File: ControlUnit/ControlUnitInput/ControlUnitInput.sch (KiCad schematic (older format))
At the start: 41 parts, among them J1 Conn_02x15_Odd_Even, J2 Conn_01x02, SW1 SW_Push, SW10 SW_Push, SW11 SW_Push, SW12 SW_Push, SW13 SW_Push, SW14 SW_Push, SW15 SW_Push, SW16 SW_Push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

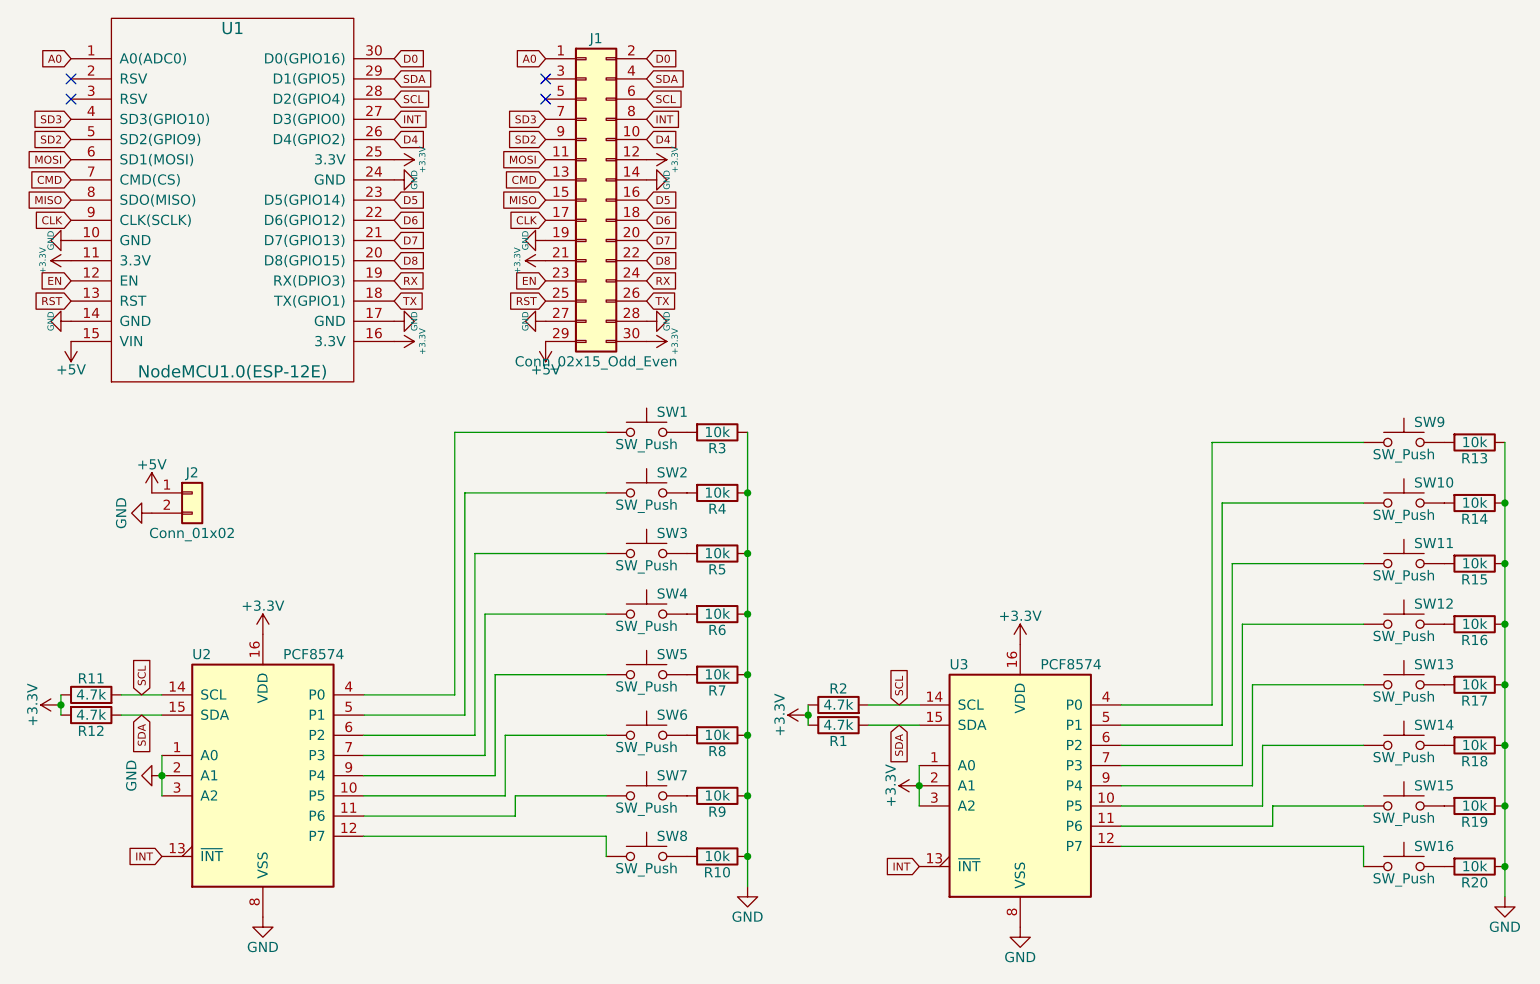
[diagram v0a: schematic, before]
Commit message: add additional connectors for NodeMCU pins in order to be able to connect additional input devices later on
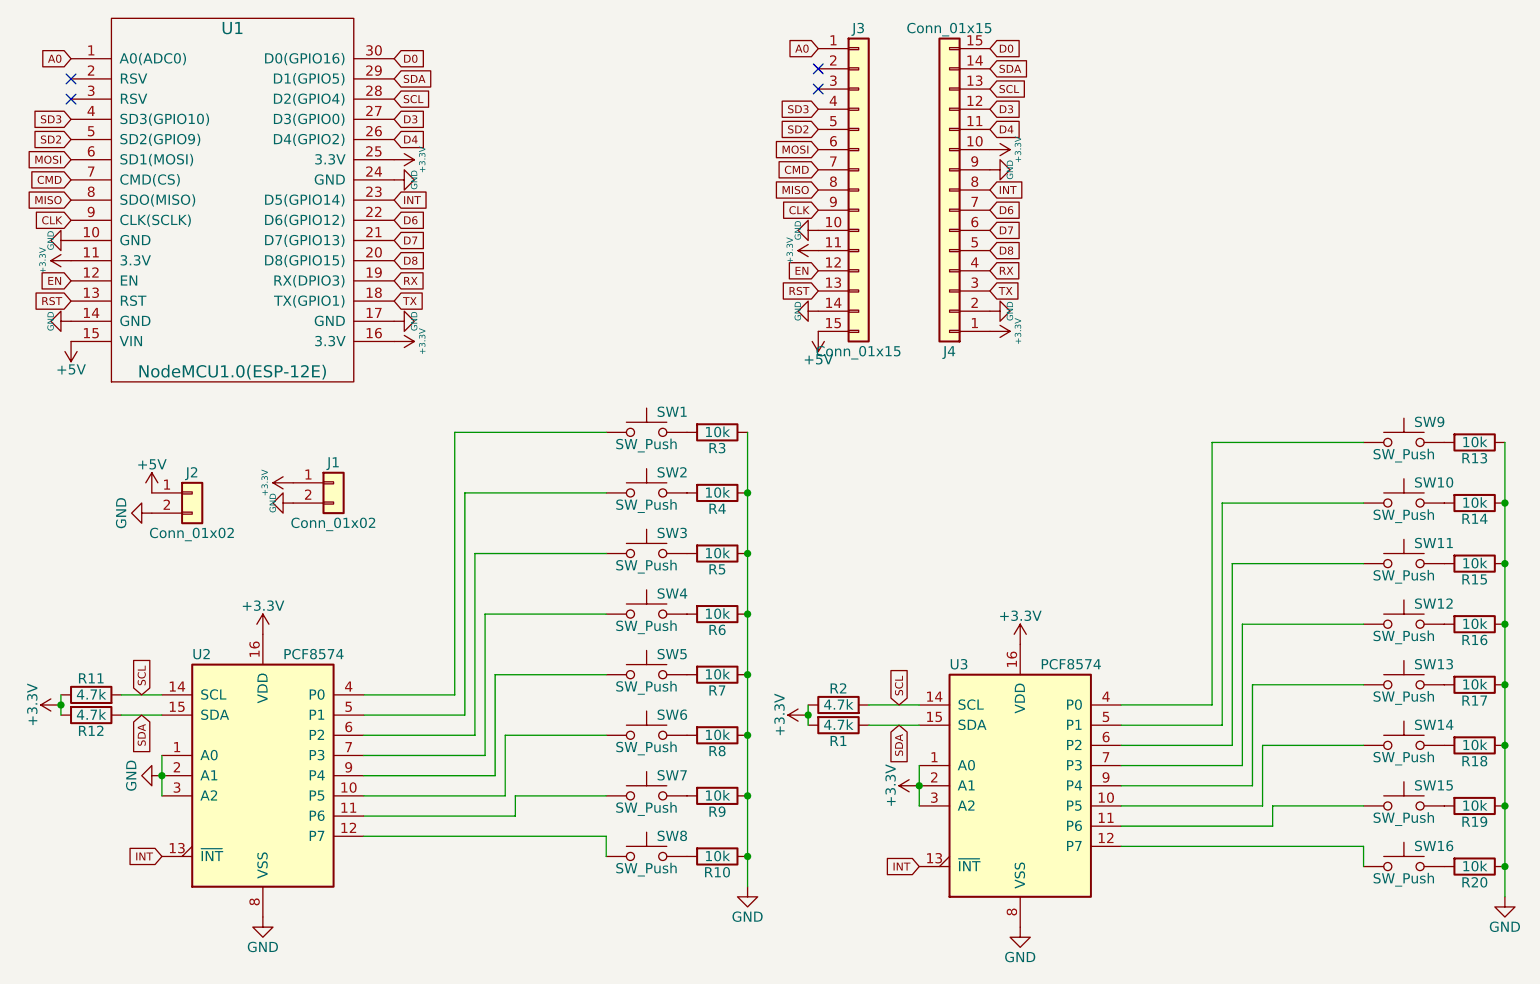
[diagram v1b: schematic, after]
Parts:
- removed J1: Conn_02x15_Odd_Even, Pin_Headers:Pin_Header_Straight_2x15_Pitch2.54mm, symbol Conn_02x15_Odd_Even
- added J1: Conn_01x02, Pin_Headers:Pin_Header_Straight_1x02_Pitch2.54mm, symbol Conn_01x02
- added J3, J4: Conn_01x15, Pin_Headers:Pin_Header_Straight_1x15_Pitch2.54mm, symbol Conn_01x15
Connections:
- net D5 is gone; now on net INT: U1.23 (D5(GPIO14))
- net +3V3: now also J1.1 (Pin_1), J3.11 (Pin_11), J4.1 (Pin_1), J4.10 (Pin_10)
- net +5V: now also J3.15 (Pin_15)
- net A0: now also J3.1 (Pin_1)
- net CLK: now also J3.9 (Pin_9)
- net CMD: now also J3.7 (Pin_7)
- net D0: now also J4.15 (Pin_15)
- net D4: now also J4.11 (Pin_11)
- net D6: now also J4.7 (Pin_7)
- net D7: now also J4.6 (Pin_6)
- net D8: now also J4.5 (Pin_5)
- net EN: now also J3.12 (Pin_12)
- net GND: now also J1.2 (Pin_2), J3.10 (Pin_10), J3.14 (Pin_14), J4.2 (Pin_2), J4.9 (Pin_9)
- net INT: now also J4.8 (Pin_8); no longer U1.27 (D3(GPIO0))
- net MISO: now also J3.8 (Pin_8)
- net MOSI: now also J3.6 (Pin_6)
- net RST: now also J3.13 (Pin_13)
- net RX: now also J4.4 (Pin_4)
- net SCL: now also J4.13 (Pin_13)
- net SD2: now also J3.5 (Pin_5)
- net SD3: now also J3.4 (Pin_4)
- net SDA: now also J4.14 (Pin_14)
- net TX: now also J4.3 (Pin_3)
- new net D3: J4.12 (Pin_12), U1.27 (D3(GPIO0))
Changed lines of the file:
@@
 LIBS:valves
 LIBS:IRLZ34
-LIBS:ws2812b
-LIBS:ESP8266
 LIBS:ControlUnitInput-cache
 EELAYER 25 0
@@
 Text GLabel 2500 950  2    39   Input ~ 0
 SCL
-Text GLabel 2500 1050 2    39   Input ~ 0
+Text GLabel 2500 1450 2    39   Input ~ 0
 INT
 Text GLabel 2500 750  2    39   Input ~ 0
@@
 Text GLabel 2500 1150 2    39   Input ~ 0
 D4
-Text GLabel 2500 1450 2    39   Input ~ 0
-D5
+Text GLabel 2500 1050 2    39   Input ~ 0
+D3
 Text GLabel 2500 1550 2    39   Input ~ 0
 D6
@@
 	0    1    1    0
 $EndComp
-$Comp
-L Conn_02x15_Odd_Even J1
-U 1 1 5A34A10D
-P 3450 1450
-F 0 "J1" H 3500 2250 50  0000 C CNN
-F 1 "Conn_02x15_Odd_Even" H 3500 650 50  0000 C CNN
-F 2 "Pin_Headers:Pin_Header_Straight_2x15_Pitch2.54mm" H 3450 1450 50  0001 C CNN
-F 3 "" H 3450 1450 50  0001 C CNN
-	1    3450 1450
-	1    0    0    -1
-$EndComp
-Text GLabel 3750 750  2    39   Input ~ 0
+Text GLabel 5450 700  2    39   Input ~ 0
 D0
-Text GLabel 3750 850  2    39   Input ~ 0
+Text GLabel 5450 800  2    39   Input ~ 0
 SDA
-Text GLabel 3750 950  2    39   Input ~ 0
+Text GLabel 5450 900  2    39   Input ~ 0
 SCL
-Text GLabel 3750 1050 2    39   Input ~ 0
+Text GLabel 5450 1400 2    39   Input ~ 0
 INT
-Text GLabel 3750 1150 2    39   Input ~ 0
+Text GLabel 5450 1100 2    39   Input ~ 0
 D4
 $Comp
 L GND #PWR06
 U 1 1 5A34A4EF
-P 3750 1350
-F 0 "#PWR06" H 3750 1100 31  0001 C CNN
-F 1 "GND" H 3750 1250 31  0000 C CNN
-F 2 "" H 3750 1350 50  0001 C CNN
-F 3 "" H 3750 1350 50  0001 C CNN
-	1    3750 1350
-	0    -1   -1   0
-$EndComp
-Text GLabel 3750 1450 2    39   Input ~ 0
-D5
-Text GLabel 3750 1550 2    39   Input ~ 0
+P 5450 1300
+F 0 "#PWR06" H 5450 1050 31  0001 C CNN
+F 1 "GND" H 5450 1200 31  0000 C CNN
+F 2 "" H 5450 1300 50  0001 C CNN
+F 3 "" H 5450 1300 50  0001 C CNN
+	1    5450 1300
+	0    -1   -1   0
+$EndComp
+Text GLabel 5450 1000 2    39   Input ~ 0
+D3
+Text GLabel 5450 1500 2    39   Input ~ 0
 D6
-Text GLabel 3750 1650 2    39   Input ~ 0
+Text GLabel 5450 1600 2    39   Input ~ 0
 D7
-Text GLabel 3750 1750 2    39   Input ~ 0
+Text GLabel 5450 1700 2    39   Input ~ 0
 D8
-Text GLabel 3750 1850 2    39   Input ~ 0
+Text GLabel 5450 1800 2    39   Input ~ 0
 RX
-Text GLabel 3750 1950 2    39   Input ~ 0
+Text GLabel 5450 1900 2    39   Input ~ 0
 TX
 $Comp
 L GND #PWR07
 U 1 1 5A34A84E
-P 3750 2050
-F 0 "#PWR07" H 3750 1800 31  0001 C CNN
-F 1 "GND" H 3750 1950 31  0000 C CNN
-F 2 "" H 3750 2050 50  0001 C CNN
-F 3 "" H 3750 2050 50  0001 C CNN
-	1    3750 2050
+P 5450 2000
+F 0 "#PWR07" H 5450 1750 31  0001 C CNN
+F 1 "GND" H 5450 1900 31  0000 C CNN
+F 2 "" H 5450 2000 50  0001 C CNN
+F 3 "" H 5450 2000 50  0001 C CNN
+	1    5450 2000
 	0    -1   -1   0
 $EndComp
@@
 L +5V #PWR08
 U 1 1 5A34A8F9
-P 3250 2150
-F 0 "#PWR08" H 3250 2000 50  0001 C CNN
-F 1 "+5V" H 3250 2290 50  0000 C CNN
-F 2 "" H 3250 2150 50  0001 C CNN
-F 3 "" H 3250 2150 50  0001 C CNN
-	1    3250 2150
+P 4600 2100
+F 0 "#PWR08" H 4600 1950 50  0001 C CNN
+F 1 "+5V" H 4600 2240 50  0000 C CNN
+F 2 "" H 4600 2100 50  0001 C CNN
+F 3 "" H 4600 2100 50  0001 C CNN
+	1    4600 2100
 	-1   0    0    1
 $EndComp
@@
 L GND #PWR09
 U 1 1 5A34A97C
-P 3250 2050
-F 0 "#PWR09" H 3250 1800 31  0001 C CNN
-F 1 "GND" H 3250 1950 31  0000 C CNN
-F 2 "" H 3250 2050 50  0001 C CNN
-F 3 "" H 3250 2050 50  0001 C CNN
-	1    3250 2050
-	0    1    1    0
-$EndComp
-Text GLabel 3250 1950 0    39   Input ~ 0
+P 4600 2000
+F 0 "#PWR09" H 4600 1750 31  0001 C CNN
+F 1 "GND" H 4600 1900 31  0000 C CNN
+F 2 "" H 4600 2000 50  0001 C CNN
+F 3 "" H 4600 2000 50  0001 C CNN
+	1    4600 2000
+	0    1    1    0
+$EndComp
+Text GLabel 4600 1900 0    39   Input ~ 0
 RST
-Text GLabel 3250 1850 0    39   Input ~ 0
+Text GLabel 4600 1800 0    39   Input ~ 0
 EN
 $Comp
 L GND #PWR010
 U 1 1 5A34AAF3
-P 3250 1650
-F 0 "#PWR010" H 3250 1400 31  0001 C CNN
-F 1 "GND" H 3250 1550 31  0000 C CNN
-F 2 "" H 3250 1650 50  0001 C CNN
-F 3 "" H 3250 1650 50  0001 C CNN
-	1    3250 1650
-	0    1    1    0
-$EndComp
-Text GLabel 3250 1550 0    39   Input ~ 0
+P 4600 1600
+F 0 "#PWR010" H 4600 1350 31  0001 C CNN
+F 1 "GND" H 4600 1500 31  0000 C CNN
+F 2 "" H 4600 1600 50  0001 C CNN
+F 3 "" H 4600 1600 50  0001 C CNN
+	1    4600 1600
+	0    1    1    0
+$EndComp
+Text GLabel 4600 1500 0    39   Input ~ 0
 CLK
-Text GLabel 3250 1450 0    39   Input ~ 0
+Text GLabel 4600 1400 0    39   Input ~ 0
 MISO
-Text GLabel 3250 1350 0    39   Input ~ 0
+Text GLabel 4600 1300 0    39   Input ~ 0
 CMD
-Text GLabel 3250 1250 0    39   Input ~ 0
+Text GLabel 4600 1200 0    39   Input ~ 0
 MOSI
-Text GLabel 3250 1150 0    39   Input ~ 0
+Text GLabel 4600 1100 0    39   Input ~ 0
 SD2
-Text GLabel 3250 1050 0    39   Input ~ 0
+Text GLabel 4600 1000 0    39   Input ~ 0
 SD3
-Text GLabel 3250 750  0    39   Input ~ 0
+Text GLabel 4600 700  0    39   Input ~ 0
 A0
 $Comp
@@
 L +3.3V #PWR014
 U 1 1 5A34BDD2
-P 3750 2150
-F 0 "#PWR014" H 3750 2000 31  0001 C CNN
-F 1 "+3.3V" H 3750 2290 31  0000 C CNN
-F 2 "" H 3750 2150 50  0001 C CNN
-F 3 "" H 3750 2150 50  0001 C CNN
-	1    3750 2150
+P 5450 2100
+F 0 "#PWR014" H 5450 1950 31  0001 C CNN
+F 1 "+3.3V" H 5450 2240 31  0000 C CNN
+F 2 "" H 5450 2100 50  0001 C CNN
+F 3 "" H 5450 2100 50  0001 C CNN
+	1    5450 2100
 	0    1    1    0
 $EndComp
@@
 L +3.3V #PWR025
 U 1 1 5A3532E4
-P 3250 1750
-F 0 "#PWR025" H 3250 1600 31  0001 C CNN
-F 1 "+3.3V" H 3250 1890 31  0000 C CNN
-F 2 "" H 3250 1750 50  0001 C CNN
-F 3 "" H 3250 1750 50  0001 C CNN
-	1    3250 1750
+P 4600 1700
+F 0 "#PWR025" H 4600 1550 31  0001 C CNN
+F 1 "+3.3V" H 4600 1840 31  0000 C CNN
+F 2 "" H 4600 1700 50  0001 C CNN
+F 3 "" H 4600 1700 50  0001 C CNN
+	1    4600 1700
 	0    -1   -1   0
 $EndComp
@@
 L +3.3V #PWR026
 U 1 1 5A353367
-P 3750 1250
-F 0 "#PWR026" H 3750 1100 31  0001 C CNN
-F 1 "+3.3V" H 3750 1390 31  0000 C CNN
-F 2 "" H 3750 1250 50  0001 C CNN
-F 3 "" H 3750 1250 50  0001 C CNN
-	1    3750 1250
-	0    1    1    0
-$EndComp
-NoConn ~ 3250 850
-NoConn ~ 3250 950
+P 5450 1200
+F 0 "#PWR026" H 5450 1050 31  0001 C CNN
+F 1 "+3.3V" H 5450 1340 31  0000 C CNN
+F 2 "" H 5450 1200 50  0001 C CNN
+F 3 "" H 5450 1200 50  0001 C CNN
+	1    5450 1200
+	0    1    1    0
+$EndComp
 NoConn ~ 900  850
 NoConn ~ 900  950
@@
 	1    0    0    -1
 $EndComp
+$Comp
+L Conn_01x15 J3
+U 1 1 5A4ABF15
+P 4800 1400
+F 0 "J3" H 4800 2200 50  0000 C CNN
+F 1 "Conn_01x15" H 4800 600 50  0000 C CNN
+F 2 "Pin_Headers:Pin_Header_Straight_1x15_Pitch2.54mm" H 4800 1400 50  0001 C CNN
+F 3 "" H 4800 1400 50  0001 C CNN
+	1    4800 1400
+	1    0    0    -1
+$EndComp
+$Comp
+L Conn_01x15 J4
+U 1 1 5A4ABFE6
+P 5250 1400
+F 0 "J4" H 5250 2200 50  0000 C CNN
+F 1 "Conn_01x15" H 5250 600 50  0000 C CNN
+F 2 "Pin_Headers:Pin_Header_Straight_1x15_Pitch2.54mm" H 5250 1400 50  0001 C CNN
+F 3 "" H 5250 1400 50  0001 C CNN
+	1    5250 1400
+	-1   0    0    1
+$EndComp
+NoConn ~ 4600 800
+NoConn ~ 4600 900
+$Comp
+L Conn_01x02 J1
+U 1 1 5A4AC288
+P 2200 2850
+F 0 "J1" H 2200 2950 50  0000 C CNN
+F 1 "Conn_01x02" H 2200 2650 50  0000 C CNN
+F 2 "Pin_Headers:Pin_Header_Straight_1x02_Pitch2.54mm" H 2200 2850 50  0001 C CNN
+F 3 "" H 2200 2850 50  0001 C CNN
+	1    2200 2850
+	1    0    0    -1
+$EndComp
+$Comp
+L +3.3V #PWR029
+U 1 1 5A4AC373
+P 2000 2850
+F 0 "#PWR029" H 2000 2700 31  0001 C CNN
+F 1 "+3.3V" H 2000 2990 31  0000 C CNN
+F 2 "" H 2000 2850 50  0001 C CNN
+F 3 "" H 2000 2850 50  0001 C CNN
+	1    2000 2850
+	0    -1   -1   0
+$EndComp
+$Comp
+L GND #PWR030
+U 1 1 5A4AC3FF
+P 2000 2950
+F 0 "#PWR030" H 2000 2700 31  0001 C CNN
+F 1 "GND" H 2000 2850 31  0000 C CNN
+F 2 "" H 2000 2950 50  0001 C CNN
+F 3 "" H 2000 2950 50  0001 C CNN
+	1    2000 2950
+	0    1    1    0
+$EndComp
 $EndSCHEMATC
